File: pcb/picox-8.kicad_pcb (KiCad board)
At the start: 2 copper layers, 287.5 x 119 mm, 0 parts

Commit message: some pcb progress
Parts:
- added J1: PX-8 Expansion Port, Connector_IDC:IDC-Header_2x25_P2.54mm_Latch_Horizontal, F.Cu at (125.2, 108.3)
- added R1: 1M, Resistor_SMD:R_0603_1608Metric_Pad0.98x0.95mm_HandSolder, B.Cu at (221.2, 124.6)
- added R10: 1M, Resistor_SMD:R_0603_1608Metric_Pad0.98x0.95mm_HandSolder, B.Cu at (193.8, 124.6)
- added R11: 3.3k, Resistor_SMD:R_0603_1608Metric_Pad0.98x0.95mm_HandSolder, B.Cu at (224.3, 121.1)
- added R12: 1M, Resistor_SMD:R_0603_1608Metric_Pad0.98x0.95mm_HandSolder, B.Cu at (224.3, 124.6)
- added R13: 3.3k, Resistor_SMD:R_0603_1608Metric_Pad0.98x0.95mm_HandSolder, B.Cu at (195.3, 121.1)
- added R14: 3.3k, Resistor_SMD:R_0603_1608Metric_Pad0.98x0.95mm_HandSolder, B.Cu at (225.8, 121.1)
- added R15: 3.3k, Resistor_SMD:R_0603_1608Metric_Pad0.98x0.95mm_HandSolder, B.Cu at (198.4, 121.1)
- added R16: 3.3k, Resistor_SMD:R_0603_1608Metric_Pad0.98x0.95mm_HandSolder, B.Cu at (227.3, 121.1)
- added R17: 3.3k, Resistor_SMD:R_0603_1608Metric_Pad0.98x0.95mm_HandSolder, B.Cu at (196.8, 121.1)
- added R18: 3.3k, Resistor_SMD:R_0603_1608Metric_Pad0.98x0.95mm_HandSolder, B.Cu at (216.7, 121.1)
- added R19: 1M, Resistor_SMD:R_0603_1608Metric_Pad0.98x0.95mm_HandSolder, B.Cu at (195.3, 124.6)
- added R2: 3.3k, Resistor_SMD:R_0603_1608Metric_Pad0.98x0.95mm_HandSolder, B.Cu at (221.2, 121.1)
- added R20: 1M, Resistor_SMD:R_0603_1608Metric_Pad0.98x0.95mm_HandSolder, B.Cu at (225.8, 124.6)
- added R21: 1M, Resistor_SMD:R_0603_1608Metric_Pad0.98x0.95mm_HandSolder, B.Cu at (198.4, 124.6)
- added R22: 1M, Resistor_SMD:R_0603_1608Metric_Pad0.98x0.95mm_HandSolder, B.Cu at (227.3, 124.6)
- added R23: 1M, Resistor_SMD:R_0603_1608Metric_Pad0.98x0.95mm_HandSolder, B.Cu at (196.8, 124.6)
- added R24: 1M, Resistor_SMD:R_0603_1608Metric_Pad0.98x0.95mm_HandSolder, B.Cu at (216.7, 124.6)
- added R25: 3.3k, Resistor_SMD:R_0603_1608Metric_Pad0.98x0.95mm_HandSolder, B.Cu at (187.7, 121.1)
- added R26: 3.3k, Resistor_SMD:R_0603_1608Metric_Pad0.98x0.95mm_HandSolder, B.Cu at (218.2, 121.1)
- added R27: 3.3k, Resistor_SMD:R_0603_1608Metric_Pad0.98x0.95mm_HandSolder, B.Cu at (189.2, 121.1)
- added R28: 3.3k, Resistor_SMD:R_0603_1608Metric_Pad0.98x0.95mm_HandSolder, B.Cu at (192.3, 121.1)
- added R29: 3.3k, Resistor_SMD:R_0603_1608Metric_Pad0.98x0.95mm_HandSolder, B.Cu at (199.9, 121.1)
- added R3: 3.3k, Resistor_SMD:R_0603_1608Metric_Pad0.98x0.95mm_HandSolder, B.Cu at (190.8, 121.1)
- added R30: 3.3k, Resistor_SMD:R_0603_1608Metric_Pad0.98x0.95mm_HandSolder, B.Cu at (228.9, 121.1)
- added R31: 1M, Resistor_SMD:R_0603_1608Metric_Pad0.98x0.95mm_HandSolder, B.Cu at (187.7, 124.6)
- added R32: 1M, Resistor_SMD:R_0603_1608Metric_Pad0.98x0.95mm_HandSolder, B.Cu at (218.2, 124.6)
- added R33: 1M, Resistor_SMD:R_0603_1608Metric_Pad0.98x0.95mm_HandSolder, B.Cu at (189.2, 124.6)
- added R34: 1M, Resistor_SMD:R_0603_1608Metric_Pad0.98x0.95mm_HandSolder, B.Cu at (192.3, 124.6)
- added R35: 1M, Resistor_SMD:R_0603_1608Metric_Pad0.98x0.95mm_HandSolder, B.Cu at (199.9, 124.6)
- added R36: 1M, Resistor_SMD:R_0603_1608Metric_Pad0.98x0.95mm_HandSolder, B.Cu at (228.9, 124.6)
- added R37: 3.3k, Resistor_SMD:R_0603_1608Metric_Pad0.98x0.95mm_HandSolder, B.Cu at (201.4, 121.1)
- added R38: 3.3k, Resistor_SMD:R_0603_1608Metric_Pad0.98x0.95mm_HandSolder, B.Cu at (230.4, 121.1)
- added R39: 3.3k, Resistor_SMD:R_0603_1608Metric_Pad0.98x0.95mm_HandSolder, B.Cu at (202.9, 121.1)
- added R4: 1M, Resistor_SMD:R_0603_1608Metric_Pad0.98x0.95mm_HandSolder, B.Cu at (190.8, 124.6)
- added R40: 3.3k, Resistor_SMD:R_0603_1608Metric_Pad0.98x0.95mm_HandSolder, B.Cu at (231.9, 121.1)
- added R41: 3.3k, Resistor_SMD:R_0603_1608Metric_Pad0.98x0.95mm_HandSolder, B.Cu at (204.5, 121.1)
- added R42: 3.3k, Resistor_SMD:R_0603_1608Metric_Pad0.98x0.95mm_HandSolder, B.Cu at (233.4, 121.1)
- added R43: 1M, Resistor_SMD:R_0603_1608Metric_Pad0.98x0.95mm_HandSolder, B.Cu at (201.4, 124.6)
- added R44: 1M, Resistor_SMD:R_0603_1608Metric_Pad0.98x0.95mm_HandSolder, B.Cu at (230.4, 124.6)
- added R45: 1M, Resistor_SMD:R_0603_1608Metric_Pad0.98x0.95mm_HandSolder, B.Cu at (202.9, 124.6)
- added R46: 1M, Resistor_SMD:R_0603_1608Metric_Pad0.98x0.95mm_HandSolder, B.Cu at (231.9, 124.6)
- added R47: 1M, Resistor_SMD:R_0603_1608Metric_Pad0.98x0.95mm_HandSolder, B.Cu at (204.5, 124.6)
- added R48: 1M, Resistor_SMD:R_0603_1608Metric_Pad0.98x0.95mm_HandSolder, B.Cu at (233.4, 124.6)
- added R49: 3.3k, Resistor_SMD:R_0603_1608Metric_Pad0.98x0.95mm_HandSolder, B.Cu at (212.1, 121.1)
- added R5: 3.3k, Resistor_SMD:R_0603_1608Metric_Pad0.98x0.95mm_HandSolder, B.Cu at (219.7, 121.1)
- added R50: 3.3k, Resistor_SMD:R_0603_1608Metric_Pad0.98x0.95mm_HandSolder, B.Cu at (210.6, 121.1)
- added R51: 3.3k, Resistor_SMD:R_0603_1608Metric_Pad0.98x0.95mm_HandSolder, B.Cu at (242.6, 121.1)
- added R52: 3.3k, Resistor_SMD:R_0603_1608Metric_Pad0.98x0.95mm_HandSolder, B.Cu at (239.5, 121.1)
- added R55: 1M, Resistor_SMD:R_0603_1608Metric_Pad0.98x0.95mm_HandSolder, B.Cu at (212.1, 124.6)
- added R56: 1M, Resistor_SMD:R_0603_1608Metric_Pad0.98x0.95mm_HandSolder, B.Cu at (210.6, 124.6)
- added R57: 1M, Resistor_SMD:R_0603_1608Metric_Pad0.98x0.95mm_HandSolder, B.Cu at (242.6, 124.6)
- added R58: 1M, Resistor_SMD:R_0603_1608Metric_Pad0.98x0.95mm_HandSolder, B.Cu at (239.5, 124.6)
- added R6: 1M, Resistor_SMD:R_0603_1608Metric_Pad0.98x0.95mm_HandSolder, B.Cu at (219.7, 124.6)
- added R61: 3.3k, Resistor_SMD:R_0603_1608Metric_Pad0.98x0.95mm_HandSolder, B.Cu at (206.0, 121.1)
- added R62: 1M, Resistor_SMD:R_0603_1608Metric_Pad0.98x0.95mm_HandSolder, B.Cu at (206.0, 124.6)
- added R63: 3.3k, Resistor_SMD:R_0603_1608Metric_Pad0.98x0.95mm_HandSolder, B.Cu at (207.5, 121.1)
- added R64: 1M, Resistor_SMD:R_0603_1608Metric_Pad0.98x0.95mm_HandSolder, B.Cu at (207.5, 124.6)
- added R65: 3.3k, Resistor_SMD:R_0603_1608Metric_Pad0.98x0.95mm_HandSolder, B.Cu at (209.0, 121.1)
- added R66: 1M, Resistor_SMD:R_0603_1608Metric_Pad0.98x0.95mm_HandSolder, B.Cu at (209.0, 124.6)
- added R67: 3.3k, Resistor_SMD:R_0603_1608Metric_Pad0.98x0.95mm_HandSolder, B.Cu at (213.6, 121.1)
- added R68: 1M, Resistor_SMD:R_0603_1608Metric_Pad0.98x0.95mm_HandSolder, B.Cu at (213.6, 124.6)
- added R69: 3.3k, Resistor_SMD:R_0603_1608Metric_Pad0.98x0.95mm_HandSolder, B.Cu at (215.1, 121.1)
- added R7: 3.3k, Resistor_SMD:R_0603_1608Metric_Pad0.98x0.95mm_HandSolder, B.Cu at (222.8, 121.1)
- added R70: 1M, Resistor_SMD:R_0603_1608Metric_Pad0.98x0.95mm_HandSolder, B.Cu at (215.1, 124.6)
- added R71: 3.3k, Resistor_SMD:R_0603_1608Metric_Pad0.98x0.95mm_HandSolder, B.Cu at (234.9, 121.1)
- added R72: 3.3k, Resistor_SMD:R_0603_1608Metric_Pad0.98x0.95mm_HandSolder, B.Cu at (236.5, 121.1)
- added R73: 3.3k, Resistor_SMD:R_0603_1608Metric_Pad0.98x0.95mm_HandSolder, B.Cu at (238.0, 121.1)
- added R74: 3.3k, Resistor_SMD:R_0603_1608Metric_Pad0.98x0.95mm_HandSolder, B.Cu at (241.0, 121.1)
- added R76: 1M, Resistor_SMD:R_0603_1608Metric_Pad0.98x0.95mm_HandSolder, B.Cu at (234.9, 124.6)
- added R77: 1M, Resistor_SMD:R_0603_1608Metric_Pad0.98x0.95mm_HandSolder, B.Cu at (236.5, 124.6)
- added R78: 1M, Resistor_SMD:R_0603_1608Metric_Pad0.98x0.95mm_HandSolder, B.Cu at (238.0, 124.6)
- added R79: 1M, Resistor_SMD:R_0603_1608Metric_Pad0.98x0.95mm_HandSolder, B.Cu at (241.0, 124.6)
- added R8: 1M, Resistor_SMD:R_0603_1608Metric_Pad0.98x0.95mm_HandSolder, B.Cu at (222.8, 124.6)
- added R9: 3.3k, Resistor_SMD:R_0603_1608Metric_Pad0.98x0.95mm_HandSolder, B.Cu at (193.8, 121.1)
- added U1: XC95144XL-TQ100, Package_QFP:TQFP-100_14x14mm_P0.5mm, B.Cu at (201.8, 153.0)
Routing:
- net /A12: track 0.00 -> 67.4 mm
- net /A14: track 0.00 -> 66.3 mm
- net /A1: track 0.00 -> 65.3 mm
- net /A15: track 0.00 -> 64.3 mm
- net /A4: track 0.00 -> 63.3 mm
- net /A6: track 0.00 -> 62.3 mm
- net /A10: track 0.00 -> 61.3 mm
- net /A8: track 0.00 -> 60.2 mm
- net /D0: track 0.00 -> 59.2 mm
- net /D2: track 0.00 -> 58.2 mm
- net /D4: track 0.00 -> 57.2 mm
- net /D6: track 0.00 -> 56.2 mm
- net /~{BUSRQ}: track 0.00 -> 55.2 mm
- net /~{M1}: track 0.00 -> 54.2 mm
- net /~{RS}: track 0.00 -> 48.1 mm
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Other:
- outline, holes or cut-outs redrawn

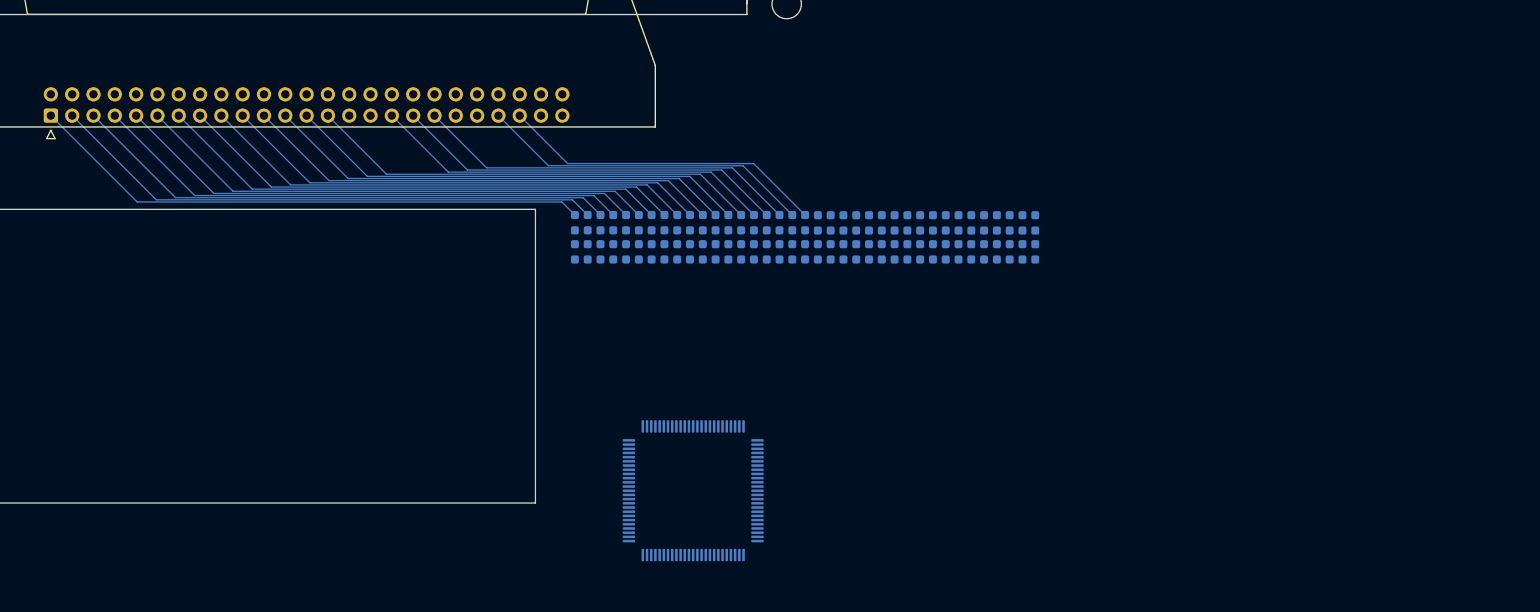
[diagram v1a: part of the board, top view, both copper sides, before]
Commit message: add bus current limiting and pull resistors
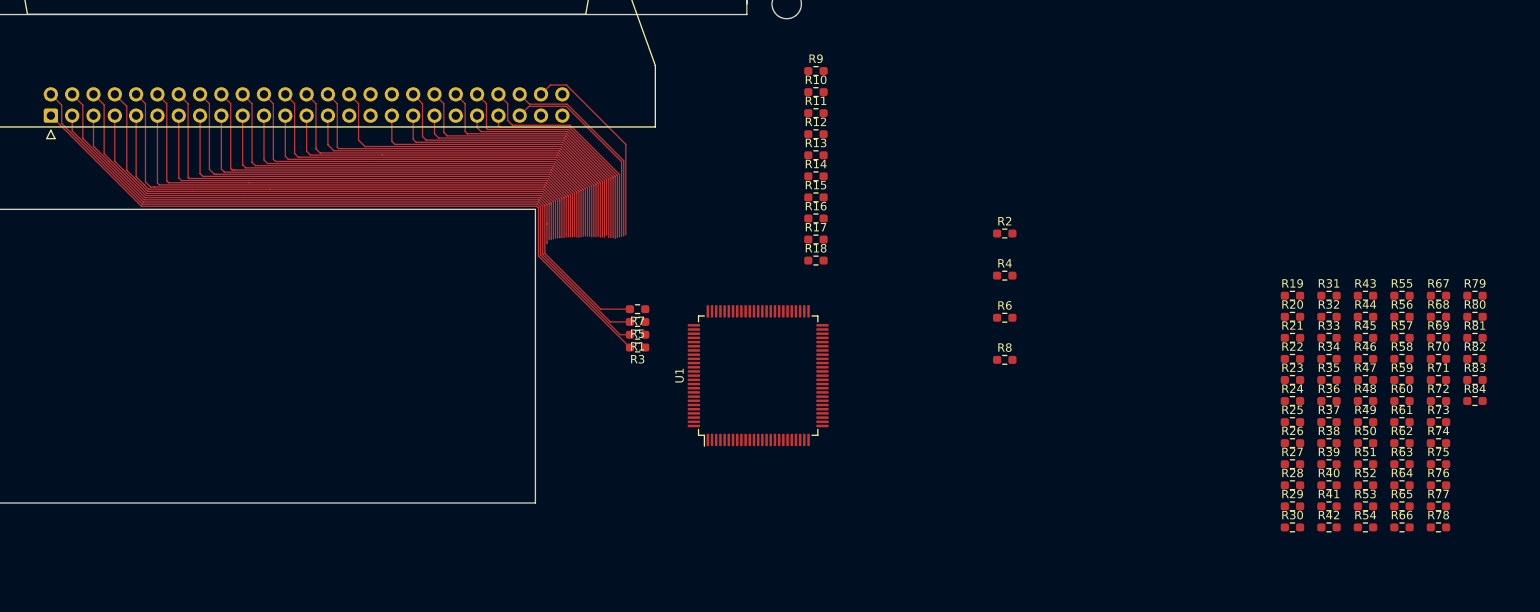
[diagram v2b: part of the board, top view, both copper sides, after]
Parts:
- added R53: 3.3k, Resistor_SMD:R_0603_1608Metric_Pad0.98x0.95mm_HandSolder, F.Cu at (281.9, 154.9)
- added R54: 1M, Resistor_SMD:R_0603_1608Metric_Pad0.98x0.95mm_HandSolder, F.Cu at (281.9, 157.4)
- added R59: 3.3k, Resistor_SMD:R_0603_1608Metric_Pad0.98x0.95mm_HandSolder, F.Cu at (286.3, 139.8)
- added R60: 1M, Resistor_SMD:R_0603_1608Metric_Pad0.98x0.95mm_HandSolder, F.Cu at (286.3, 142.3)
- added R75: 3.3k, Resistor_SMD:R_0603_1608Metric_Pad0.98x0.95mm_HandSolder, F.Cu at (290.6, 149.9)
- added R80: 1M, Resistor_SMD:R_0603_1608Metric_Pad0.98x0.95mm_HandSolder, F.Cu at (295.0, 132.3)
- added R81: 3.3k, Resistor_SMD:R_0603_1608Metric_Pad0.98x0.95mm_HandSolder, F.Cu at (295.0, 134.8)
- added R82: 1M, Resistor_SMD:R_0603_1608Metric_Pad0.98x0.95mm_HandSolder, F.Cu at (295.0, 137.3)
- added R83: 3.3k, Resistor_SMD:R_0603_1608Metric_Pad0.98x0.95mm_HandSolder, F.Cu at (295.0, 139.8)
- added R84: 1M, Resistor_SMD:R_0603_1608Metric_Pad0.98x0.95mm_HandSolder, F.Cu at (295.0, 142.3)
- R1, R19, R21, R23, R31, R33, R35, R43, R45, R47, R55, R57, R77, R79: value 1M -> 3.3k; moved to F.Cu
- R10, R11, R12, R13, R15, R17, R20, R22, R24, R25, R27, R29, R3, R32, R34, R36, R37, R39, R4, R41, R44, R46, R48, R49, R5, R51, R56, R58, R6, R61, R62, R63, R64, R65, R66, R67, R68, R69, R7, R70, R71, R73, R76, R78, R8, R9, U1: moved to F.Cu
- R14, R16, R18, R2, R26, R28, R30, R38, R40, R42, R50, R52, R72, R74: value 3.3k -> 1M; moved to F.Cu
- moved R31 90.0 mm to (277.6, 129.8), turned to 0 degrees
- moved R33 88.9 mm to (277.6, 134.8), turned to 0 degrees
- moved R27 88.8 mm to (273.2, 149.9), turned to 0 degrees
- moved R25 88.8 mm to (273.2, 144.9), turned to 0 degrees
- moved R28 86.8 mm to (273.2, 152.4), turned to 0 degrees
- moved R34 86.2 mm to (277.6, 137.3), turned to 0 degrees
- moved R65 84.3 mm to (286.3, 154.9), turned to 0 degrees
- moved R66 83.9 mm to (286.3, 157.4), turned to 0 degrees
- moved R63 83.9 mm to (286.3, 149.9), turned to 0 degrees
- moved R61 83.7 mm to (286.3, 144.9), turned to 0 degrees
- moved R64 83.5 mm to (286.3, 152.4), turned to 0 degrees
- moved R62 83.5 mm to (286.3, 147.4), turned to 0 degrees
- moved R29 80.7 mm to (273.2, 154.9), turned to 0 degrees
- moved R43 80.7 mm to (281.9, 129.8), turned to 0 degrees
- moved R41 80.5 mm to (277.6, 154.9), turned to 0 degrees
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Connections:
- R1 pad 1: /BA0 -> /BA11
- R1 pad 2: GND -> /A11
- R10 pad 1: /BA4 -> /BA1
- R11 pad 1: /BA5 -> /BA2
- R11 pad 2: /A5 -> /A2
- R12 pad 1: /BA5 -> /BA2
- R13 pad 1: /BA6 -> /BA15
- R13 pad 2: /A6 -> /A15
- R14 pad 1: /BA7 -> /BA15
- R14 pad 2: /A7 -> GND
- R15 pad 1: /BA8 -> /BA0
- R15 pad 2: /A8 -> /A0
- R16 pad 1: /BA9 -> /BA0
- R16 pad 2: /A9 -> GND
- R17 pad 1: /BA10 -> /BA4
- R17 pad 2: /A10 -> /A4
- R18 pad 1: /BA11 -> /BA4
- R18 pad 2: /A11 -> GND
- R19 pad 1: /BA6 -> /BA3
- R19 pad 2: GND -> /A3
- R2 pad 1: /BA0 -> /BA11
- R2 pad 2: /A0 -> GND
- R20 pad 1: /BA7 -> /BA3
- R21 pad 1: /BA8 -> /BA6
- R21 pad 2: GND -> /A6
- R22 pad 1: /BA9 -> /BA6
- R23 pad 1: /BA10 -> /BA5
- R23 pad 2: GND -> /A5
- R24 pad 1: /BA11 -> /BA5
- R25 pad 1: /BA12 -> /BA10
- R25 pad 2: /A12 -> /A10
- R26 pad 1: /BA13 -> /BA10
- R26 pad 2: /A13 -> GND
- R27 pad 1: /BA14 -> /BA7
- R27 pad 2: /A14 -> /A7
- R28 pad 1: /BA15 -> /BA7
- R28 pad 2: /A15 -> GND
- R29 pad 1: /BD0 -> /BA8
- R29 pad 2: /D0 -> /A8
- R3 pad 1: /BA1 -> /BA12
- R3 pad 2: /A1 -> /A12
- R30 pad 1: /BD1 -> /BA8
- R30 pad 2: /D1 -> GND
- R31 pad 1: /BA12 -> /BA9
- R31 pad 2: GND -> /A9
- R32 pad 1: /BA13 -> /BA9
- R33 pad 1: /BA14 -> /BD0
- R33 pad 2: GND -> /D0
- R34 pad 1: /BA15 -> /BD0
- R35 pad 1: /BD0 -> /BD1
- R35 pad 2: GND -> /D1
- R38 pad 1: /BD3 -> /BD2
- R38 pad 2: /D3 -> GND
- R39 pad 1: /BD4 -> /BD3
- R39 pad 2: /D4 -> /D3
- R4 pad 1: /BA1 -> /BA12
- R40 pad 1: /BD5 -> /BD3
- R40 pad 2: /D5 -> GND
- R41 pad 1: /BD6 -> /BD4
- R41 pad 2: /D6 -> /D4
- R42 pad 1: /BD7 -> /BD4
- R42 pad 2: /D7 -> GND
- R43 pad 1: /BD2 -> /BD5
- R43 pad 2: GND -> /D5
- R44 pad 1: /BD3 -> /BD5
- R45 pad 1: /BD4 -> /BD6
- R45 pad 2: GND -> /D6
- R46 pad 1: /BD5 -> /BD6
- R47 pad 1: /BD6 -> /BD7
- R47 pad 2: GND -> /D7
- R49 pad 1: /B~{WR} -> /B~{BUSRQ}
- R49 pad 2: /~{WR} -> /~{BUSRQ}
- R5 pad 1: /BA2 -> /BA14
- R5 pad 2: /A2 -> /A14
- R50 pad 1: /B~{RD} -> /B~{BUSRQ}
- R50 pad 2: /~{RD} -> GND
- R51 pad 1: /B~{IORQ} -> /B~{BUSAK}
- R51 pad 2: /~{IORQ} -> /~{BUSAK}
- R52 pad 1: /B~{MREQ} -> /B~{BUSAK}
- R52 pad 2: /~{MREQ} -> GND
- R55 pad 1: /B~{WR} -> /B~{WAIT}
- R55 pad 2: GND -> /~{WAIT}
- R56 pad 1: /B~{RD} -> /B~{WAIT}
- R57 pad 1: /B~{IORQ} -> /B~{HLTA}
- R57 pad 2: GND -> /~{HLTA}
- R58 pad 1: /B~{MREQ} -> /B~{HLTA}
- R6 pad 1: /BA2 -> /BA14
- R61 pad 1: /B~{BUSRQ} -> /B~{RD}
- R61 pad 2: /~{BUSRQ} -> /~{RD}
- R62 pad 1: /B~{BUSRQ} -> /B~{RD}
- R63 pad 1: /B~{M1} -> /B~{MREQ}
- R63 pad 2: /~{M1} -> /~{MREQ}
- R64 pad 1: /B~{M1} -> /B~{MREQ}
- R65 pad 1: /B~{RS} -> /B~{WR}
- R65 pad 2: /~{RS} -> /~{WR}
- R66 pad 1: /B~{RS} -> /B~{WR}
- R67 pad 1: /B~{INTEX} -> /B~{CLK}
- R67 pad 2: /~{INTEX} -> /~{CLK}
- R68 pad 1: /B~{INTEX} -> /B~{CLK}
- R69 pad 1: /B~{RXD} -> /B~{IORQ}
- R69 pad 2: /~{RXD} -> /~{IORQ}
- R7 pad 1: /BA3 -> /BA13
- R7 pad 2: /A3 -> /A13
- R70 pad 1: /B~{RXD} -> /B~{IORQ}
- R71 pad 1: /B~{BUSAK} -> /BDCAS
- R71 pad 2: /~{BUSAK} -> /DCAS
- R72 pad 1: /B~{WAIT} -> /BDCAS
- R72 pad 2: /~{WAIT} -> GND
- R73 pad 1: /B~{HLTA} -> /BDW
- R73 pad 2: /~{HLTA} -> /DW
- R74 pad 1: /B~{CLK} -> /BDW
- R74 pad 2: /~{CLK} -> GND
- R76 pad 1: /B~{BUSAK} -> /B~{INTEX}
- R77 pad 1: /B~{WAIT} -> /BOFF
- R77 pad 2: GND -> /OFF
- R78 pad 1: /B~{HLTA} -> /BOFF
- R79 pad 1: /B~{CLK} -> /B~{RXD}
- R79 pad 2: GND -> /~{RXD}
- R8 pad 1: /BA3 -> /BA13
- R9 pad 1: /BA4 -> /BA1
- R9 pad 2: /A4 -> /A1
- U1 pad 22: unconnected-(U1-I/O/GCK1-Pad22) -> /B~{CLK}
- U1 pad 34: unconnected-(U1-P34-Pad34) -> /B~{BK2}
- U1 pad 35: unconnected-(U1-P35-Pad35) -> /B~{TXD}
- U1 pad 36: unconnected-(U1-P36-Pad36) -> /B~{RXD}
- U1 pad 37: unconnected-(U1-P37-Pad37) -> /BOFF
- U1 pad 39: unconnected-(U1-P39-Pad39) -> /B~{INTEX}
- U1 pad 40: unconnected-(U1-P40-Pad40) -> /BDW
- U1 pad 41: unconnected-(U1-P41-Pad41) -> /BDCAS
- U1 pad 42: unconnected-(U1-P42-Pad42) -> /B~{IORQ}
- U1 pad 43: unconnected-(U1-P43-Pad43) -> /B~{WR}
- U1 pad 46: unconnected-(U1-P46-Pad46) -> /B~{MREQ}
- U1 pad 49: unconnected-(U1-P49-Pad49) -> /B~{RD}
- U1 pad 50: unconnected-(U1-P50-Pad50) -> /B~{RS}
- U1 pad 52: unconnected-(U1-P52-Pad52) -> /B~{HLTA}
- U1 pad 53: unconnected-(U1-P53-Pad53) -> /B~{WAIT}
- U1 pad 54: unconnected-(U1-P54-Pad54) -> /B~{M1}
- U1 pad 55: unconnected-(U1-P55-Pad55) -> /B~{BUSAK}
- U1 pad 56: unconnected-(U1-P56-Pad56) -> /B~{BUSRQ}
- U1 pad 58: unconnected-(U1-P58-Pad58) -> /BD7
- U1 pad 59: unconnected-(U1-P59-Pad59) -> /BD6
- U1 pad 60: unconnected-(U1-P60-Pad60) -> /BD5
- U1 pad 61: unconnected-(U1-P61-Pad61) -> /BD4
- U1 pad 63: unconnected-(U1-P63-Pad63) -> /BD3
- U1 pad 64: unconnected-(U1-P64-Pad64) -> /BD2
- U1 pad 65: unconnected-(U1-P65-Pad65) -> /BD1
- U1 pad 66: unconnected-(U1-P66-Pad66) -> /BD0
- U1 pad 67: unconnected-(U1-P67-Pad67) -> /BA9
- U1 pad 68: unconnected-(U1-P68-Pad68) -> /BA8
- U1 pad 70: unconnected-(U1-P70-Pad70) -> /BA7
- U1 pad 71: unconnected-(U1-P71-Pad71) -> /BA10
- U1 pad 72: unconnected-(U1-P72-Pad72) -> /BA5
- U1 pad 73: unconnected-(U1-P73-Pad73) -> /BA6
- U1 pad 74: unconnected-(U1-P74-Pad74) -> /BA3
- U1 pad 76: /BA11 -> /BA4
- U1 pad 77: /BA13 -> /BA0
- U1 pad 78: /BA2 -> /BA15
- U1 pad 79: /BA0 -> /BA2
- U1 pad 80: /BA3 -> /BA1
- U1 pad 81: /BA5 -> /BA13
- U1 pad 82: unconnected-(U1-P82-Pad82) -> /BA14
- U1 pad 85: unconnected-(U1-P85-Pad85) -> /BA11
- U1 pad 86: unconnected-(U1-P86-Pad86) -> /BA12
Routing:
- net /A11: track 0.00 -> 85.5 mm
- net /A13: track 0.00 -> 82.8 mm
- net /A2: track 0.00 -> 67.4 mm
- net /A0: track 0.00 -> 66.5 mm
- net /A3: track 0.00 -> 65.4 mm
- net /A5: track 0.00 -> 63.4 mm
- net /A7: track 0.00 -> 61.2 mm
- net /A9: track 0.00 -> 58.7 mm
- net /D1: track 0.00 -> 56.7 mm
- net /D3: track 0.00 -> 54.4 mm
- net /D5: track 0.00 -> 52.2 mm
- net /D7: track 0.00 -> 49.9 mm
- net /~{BUSAK}: track 0.00 -> 47.7 mm
- net /~{WAIT}: track 0.00 -> 45.7 mm
- net /~{HLTA}: track 0.00 -> 42.9 mm
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
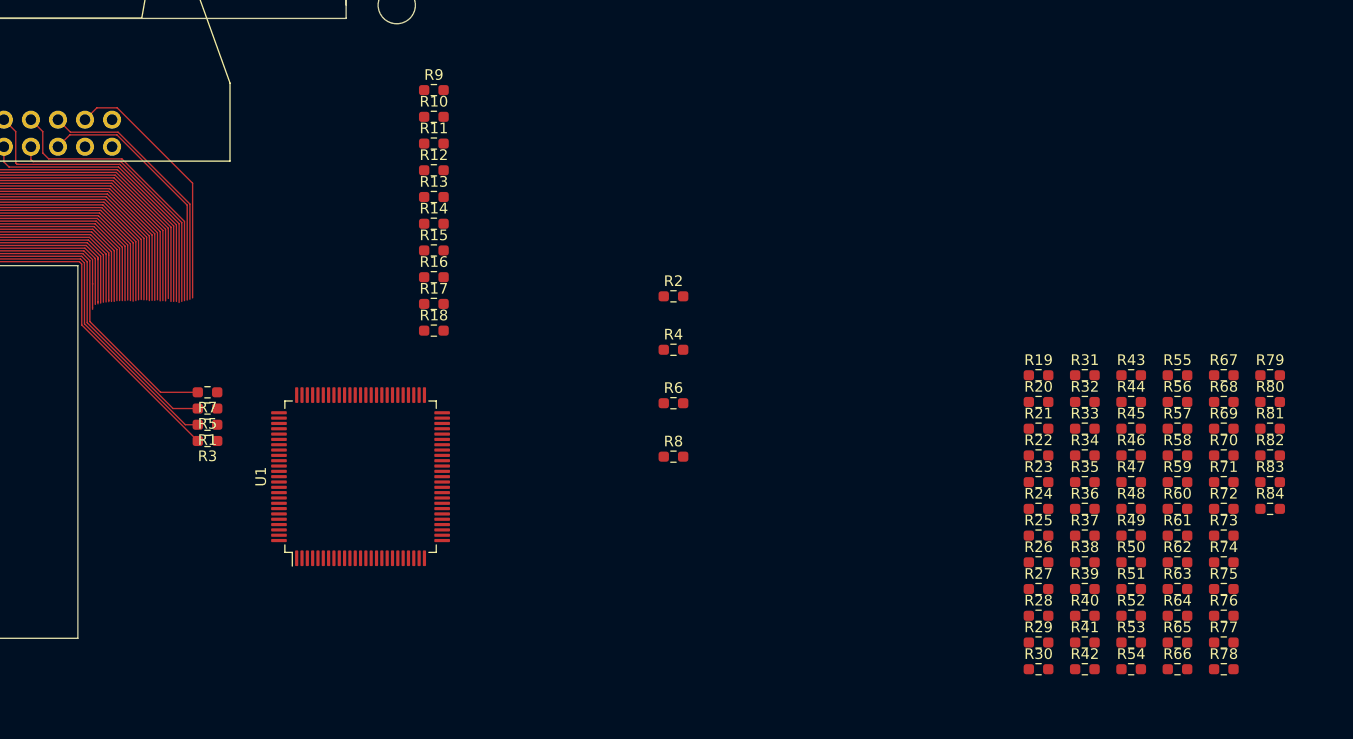
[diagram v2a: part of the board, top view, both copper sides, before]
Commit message: bus buffer resistors
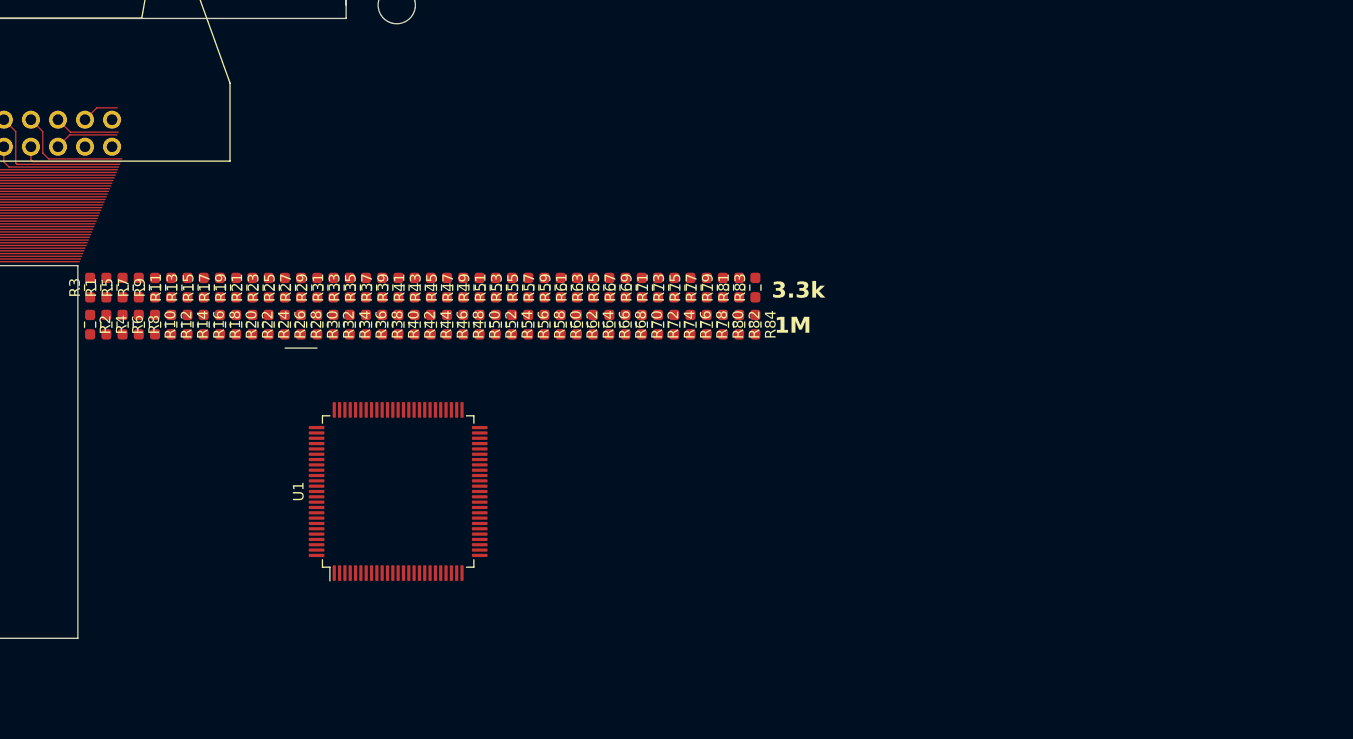
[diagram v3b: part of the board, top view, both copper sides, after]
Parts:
- moved R19 75.8 mm to (197.9, 121.6), turned to 90 degrees
- moved R20 75.7 mm to (197.9, 125.0), turned to -90 degrees
- moved R29 75.5 mm to (205.5, 121.6), turned to 90 degrees
- moved R30 75.1 mm to (205.5, 125.0), turned to -90 degrees
- moved R21 75.0 mm to (199.4, 121.6), turned to 90 degrees
- moved R22 74.9 mm to (199.4, 125.0), turned to -90 degrees
- moved R27 74.8 mm to (204.0, 121.6), turned to 90 degrees
- moved R23 74.6 mm to (200.9, 121.6), turned to 90 degrees
- moved R25 74.5 mm to (202.4, 121.6), turned to 90 degrees
- moved R28 74.5 mm to (204.0, 125.0), turned to -90 degrees
- moved R24 74.4 mm to (200.9, 125.0), turned to -90 degrees
- moved R26 74.2 mm to (202.4, 125.0), turned to -90 degrees
- moved R41 71.2 mm to (214.6, 121.6), turned to 90 degrees
- moved R31 71.0 mm to (207.0, 121.6), turned to 90 degrees
- moved R32 70.9 mm to (207.0, 125.0), turned to -90 degrees
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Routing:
- net /A12: track 83.8 -> 62.4 mm
- net /A11: track 85.5 -> 64.7 mm
- net /~{BK2}: track 24.3 -> 3.49 mm
- net /A14: track 81.1 -> 60.9 mm
- net /A13: track 82.8 -> 63.2 mm
- net /~{TXD}: track 24.6 -> 6.13 mm
- net /~{RXD}: track 24.3 -> 6.00 mm
- net /OFF: track 27.0 -> 11.3 mm
- net /~{INTEX}: track 25.2 -> 9.73 mm
- net /DW: track 29.6 -> 14.3 mm
- net /DCAS: track 27.3 -> 12.4 mm
- net /~{IORQ}: track 31.7 -> 17.1 mm
- net /~{CLK}: track 33.9 -> 19.7 mm
- net /~{WR}: track 31.6 -> 17.9 mm
- net /~{MREQ}: track 36.1 -> 22.5 mm
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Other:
- outline, holes or cut-outs redrawn
- board text added: "1M"
- board text added: "3.3k"
